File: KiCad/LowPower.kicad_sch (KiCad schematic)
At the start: 35 parts, among them J1 Connector, J2 USB-C, J3 DC, U1 ESP32-WROOM-32, U2 FT231XQ, U4 LMR16006+FB

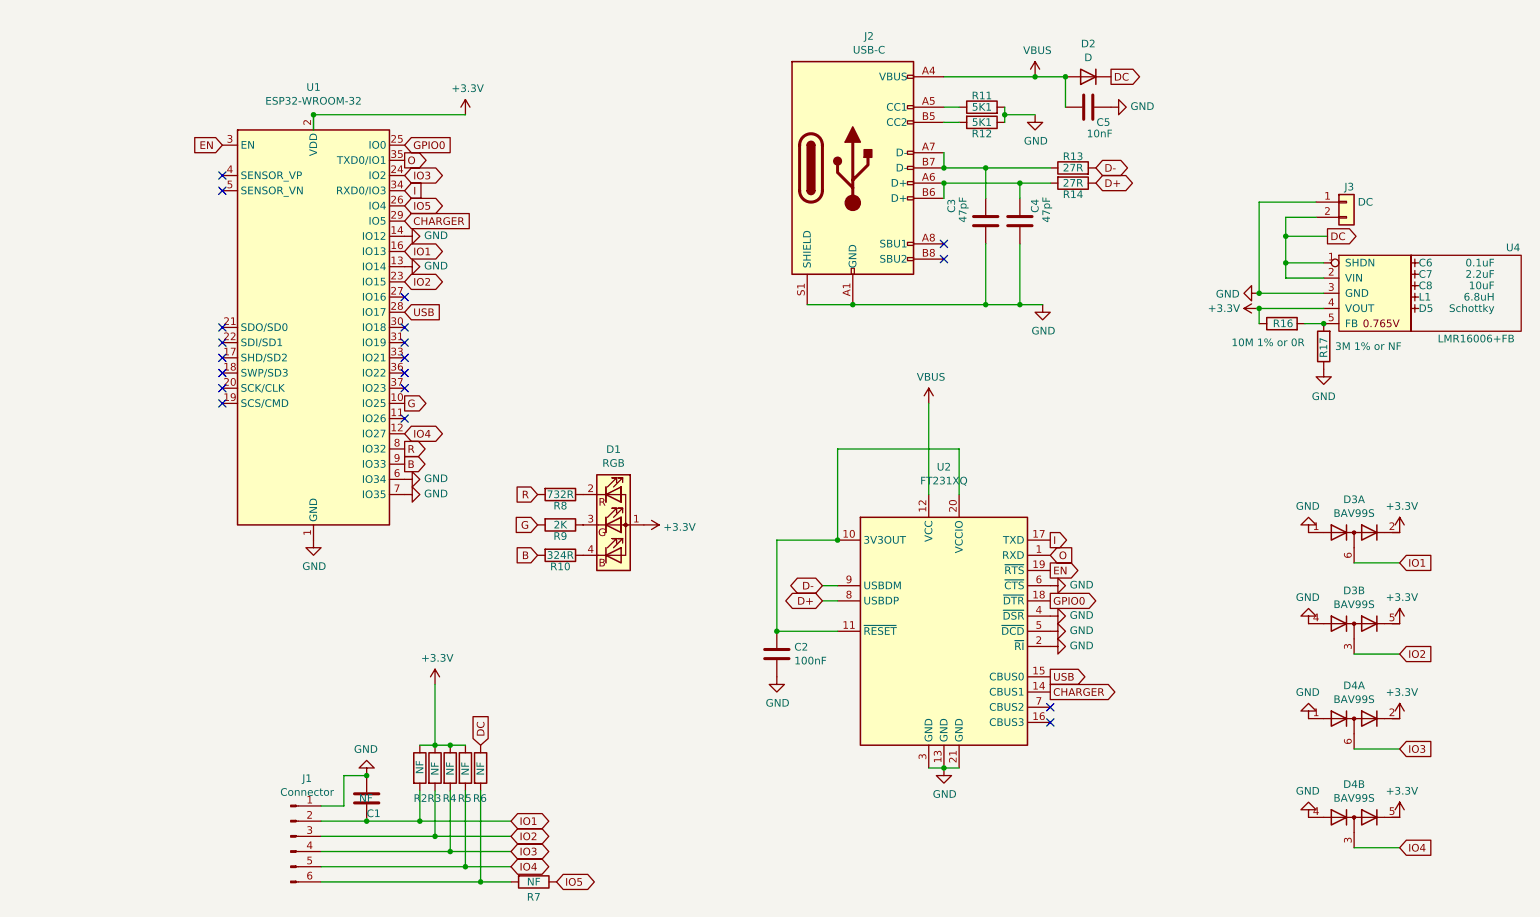
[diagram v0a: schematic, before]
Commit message: Separate Generic and LowPower boards
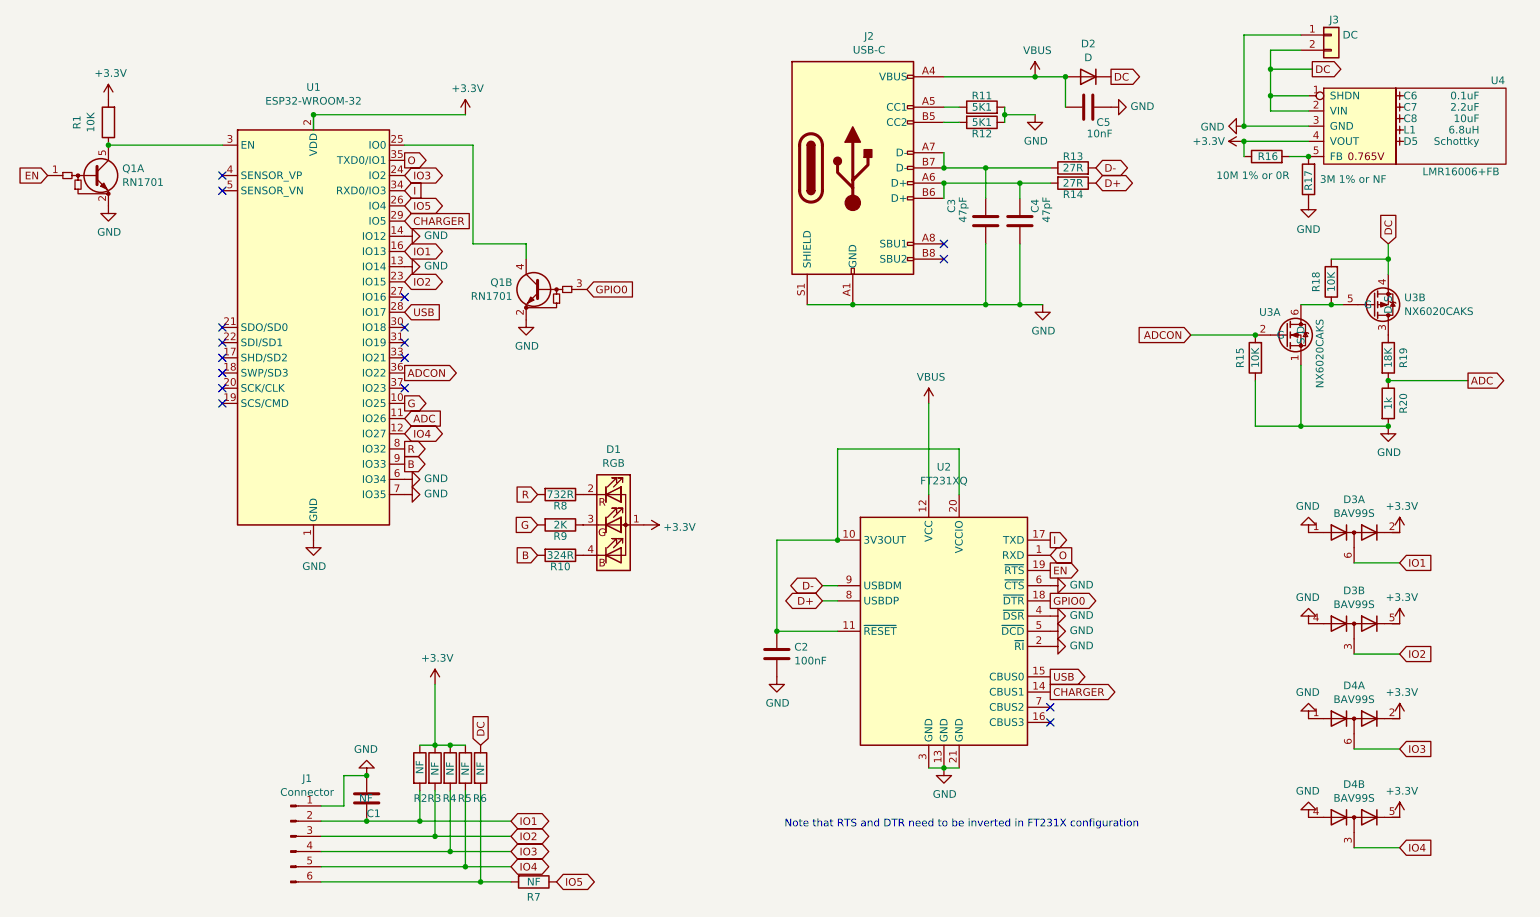
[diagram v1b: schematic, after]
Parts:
- added Q1: RN1701, RevK:USV-5, symbol RevK:RN1701
- added R1, R15, R18: 10K, RevK:R_0603, symbol Device:R
- added R19: 18K, RevK:R_0603, symbol Device:R
- added R20: 1k, RevK:R_0603, symbol Device:R
- added U3: NX6020CAKS, Package_TO_SOT_SMD:SOT-363_SC-70-6, symbol RevK:NX6020CAKS
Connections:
- net +3V3: now also R1.2
- net DC: now also R18.2, U3.4 (S)
- net EN: now also Q1.1 (B2); no longer U1.3 (EN)
- net GND: now also Q1.2 (E), Q1.2 (E), R15.1, R20.2, U3.1 (S)
- net GPIO0: now also Q1.3 (B2); no longer U1.25 (IO0)
- net ADC: now reaches U1.11 (IO26)
- net ADC: now also R19.2, R20.1
- net ADCON: now reaches U1.36 (IO22)
- net ADCON: now also R15.2, U3.2 (G)
- new net: Q1.4 (C2), U1.25 (IO0)
- new net: Q1.5 (C2), R1.1, U1.3 (EN)
- new net: R19.1, U3.3 (D)
- new net: R18.1, U3.5 (G), U3.6 (D)
- no-connect marks 19 -> 17
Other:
- note added: "Note that RTS and DTR need to be inverted in FT231X configuration"
- title: Generic ESP32 module -> Generic ESP32 (suitable for battery operation)
- moved on the sheet: C6, C7, C8, D5, J3, L1, R16, R17, U4

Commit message: New bigger generic and tidy library
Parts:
- C1, R2, R4, R5, R6, R7: footprint RevK:Pad_1206_0805_NF -> RevK:Pad_1206_0805_Open; now left out of the parts list
- R3: footprint RevK:Pad_1206_0805_NF -> RevK:Pad_1206_0805_Open
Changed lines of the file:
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@@
   )
   (symbol (lib_id "Device:R") (at 83.185 140.97 0) (unit 1)
-    (in_bom yes) (on_board yes)
+    (in_bom no) (on_board yes)
     (property "Reference" "R2" (id 0) (at 84.455 146.05 0)
       (effects (font (size 1.27 1.27)) (justify right))
@@
       (effects (font (size 1.27 1.27)) (justify right))
     )
-    (property "Footprint" "RevK:Pad_1206_0805_NF" (id 2) (at 81.407 140.97 90)
+    (property "Footprint" "RevK:Pad_1206_0805_Open" (id 2) (at 81.407 140.97 90)
       (effects (font (size 1.27 1.27)) hide)
     )
@@
       (effects (font (size 1.27 1.27)) (justify left))
     )
-    (property "Footprint" "RevK:Pad_1206_0805_NF" (id 2) (at 83.947 140.97 90)
+    (property "Footprint" "RevK:Pad_1206_0805_Open" (id 2) (at 83.947 140.97 90)
       (effects (font (size 1.27 1.27)) hide)
     )
@@
   )
   (symbol (lib_id "Device:R") (at 88.265 140.97 0) (unit 1)
-    (in_bom yes) (on_board yes)
+    (in_bom no) (on_board yes)
     (property "Reference" "R4" (id 0) (at 86.995 146.05 0)
       (effects (font (size 1.27 1.27)) (justify left))
@@
       (effects (font (size 1.27 1.27)) (justify left))
     )
-    (property "Footprint" "RevK:Pad_1206_0805_NF" (id 2) (at 86.487 140.97 90)
+    (property "Footprint" "RevK:Pad_1206_0805_Open" (id 2) (at 86.487 140.97 90)
       (effects (font (size 1.27 1.27)) hide)
     )
@@
   )
   (symbol (lib_id "Device:R") (at 90.805 140.97 0) (unit 1)
-    (in_bom yes) (on_board yes)
+    (in_bom no) (on_board yes)
     (property "Reference" "R5" (id 0) (at 89.535 146.05 0)
       (effects (font (size 1.27 1.27)) (justify left))
@@
       (effects (font (size 1.27 1.27)) (justify left))
     )
-    (property "Footprint" "RevK:Pad_1206_0805_NF" (id 2) (at 89.027 140.97 90)
+    (property "Footprint" "RevK:Pad_1206_0805_Open" (id 2) (at 89.027 140.97 90)
       (effects (font (size 1.27 1.27)) hide)
     )
@@
   )
   (symbol (lib_id "Device:R") (at 93.345 140.97 0) (unit 1)
-    (in_bom yes) (on_board yes)
+    (in_bom no) (on_board yes)
     (property "Reference" "R6" (id 0) (at 92.075 146.05 0)
       (effects (font (size 1.27 1.27)) (justify left))
@@
       (effects (font (size 1.27 1.27)) (justify left))
     )
-    (property "Footprint" "RevK:Pad_1206_0805_NF" (id 2) (at 91.567 140.97 90)
+    (property "Footprint" "RevK:Pad_1206_0805_Open" (id 2) (at 91.567 140.97 90)
       (effects (font (size 1.27 1.27)) hide)
     )
@@
   )
   (symbol (lib_id "Device:R") (at 102.235 160.02 270) (unit 1)
-    (in_bom yes) (on_board yes)
+    (in_bom no) (on_board yes)
     (property "Reference" "R7" (id 0) (at 102.235 162.56 90))
     (property "Value" "NF" (id 1) (at 102.235 160.02 90))
-    (property "Footprint" "RevK:Pad_1206_0805_NF" (id 2) (at 102.235 158.242 90)
+    (property "Footprint" "RevK:Pad_1206_0805_Open" (id 2) (at 102.235 158.242 90)
       (effects (font (size 1.27 1.27)) hide)
     )
@@
   )
   (symbol (lib_id "Device:C") (at 74.295 146.05 0) (unit 1)
-    (in_bom yes) (on_board yes)
+    (in_bom no) (on_board yes)
     (property "Reference" "C1" (id 0) (at 74.295 148.59 0)
       (effects (font (size 1.27 1.27)) (justify left))
@@
       (effects (font (size 1.27 1.27)) (justify left))
     )
-    (property "Footprint" "RevK:Pad_1206_0805_NF" (id 2) (at 75.2602 149.86 0)
+    (property "Footprint" "RevK:Pad_1206_0805_Open" (id 2) (at 75.2602 149.86 0)
       (effects (font (size 1.27 1.27)) hide)
     )
@@
     )
     (path "/00000000-0000-0000-0000-000060d24a40"
-      (reference "C1") (unit 1) (value "NF") (footprint "RevK:Pad_1206_0805_NF")
+      (reference "C1") (unit 1) (value "NF") (footprint "RevK:Pad_1206_0805_Open")
     )
     (path "/00000000-0000-0000-0000-0000609259a6"
@@
     )
     (path "/00000000-0000-0000-0000-00006043ffad"
-      (reference "R2") (unit 1) (value "NF") (footprint "RevK:Pad_1206_0805_NF")
+      (reference "R2") (unit 1) (value "NF") (footprint "RevK:Pad_1206_0805_Open")
     )
     (path "/00000000-0000-0000-0000-00006043ffb3"
-      (reference "R3") (unit 1) (value "NF") (footprint "RevK:Pad_1206_0805_NF")
+      (reference "R3") (unit 1) (value "NF") (footprint "RevK:Pad_1206_0805_Open")
     )
     (path "/00000000-0000-0000-0000-00006043ffb9"
-      (reference "R4") (unit 1) (value "NF") (footprint "RevK:Pad_1206_0805_NF")
+      (reference "R4") (unit 1) (value "NF") (footprint "RevK:Pad_1206_0805_Open")
     )
     (path "/00000000-0000-0000-0000-000060d24a3a"
-      (reference "R5") (unit 1) (value "NF") (footprint "RevK:Pad_1206_0805_NF")
+      (reference "R5") (unit 1) (value "NF") (footprint "RevK:Pad_1206_0805_Open")
     )
     (path "/00000000-0000-0000-0000-000060d24a3b"
-      (reference "R6") (unit 1) (value "NF") (footprint "RevK:Pad_1206_0805_NF")
+      (reference "R6") (unit 1) (value "NF") (footprint "RevK:Pad_1206_0805_Open")
     )
     (path "/00000000-0000-0000-0000-000060d24a3f"
-      (reference "R7") (unit 1) (value "NF") (footprint "RevK:Pad_1206_0805_NF")
+      (reference "R7") (unit 1) (value "NF") (footprint "RevK:Pad_1206_0805_Open")
     )
     (path "/00000000-0000-0000-0000-000060cf9e4d"

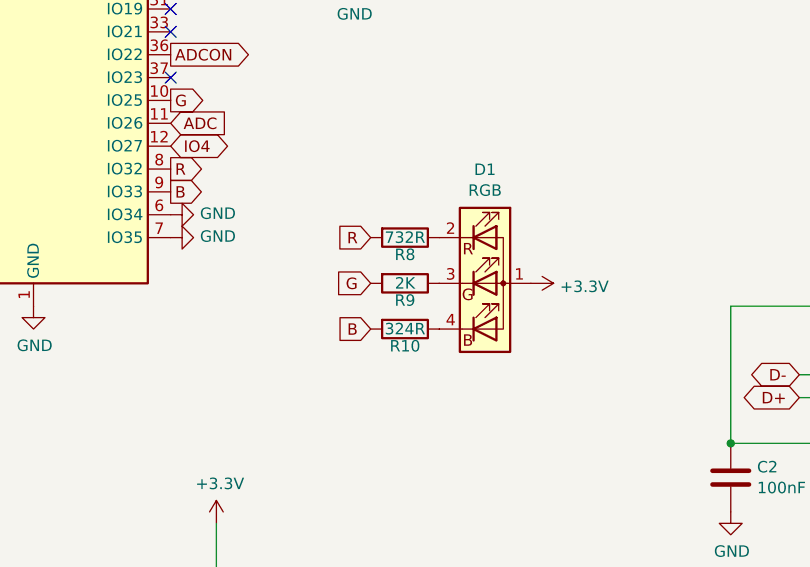
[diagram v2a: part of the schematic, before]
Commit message: Lots of tidy - mainly silkscreen stuff
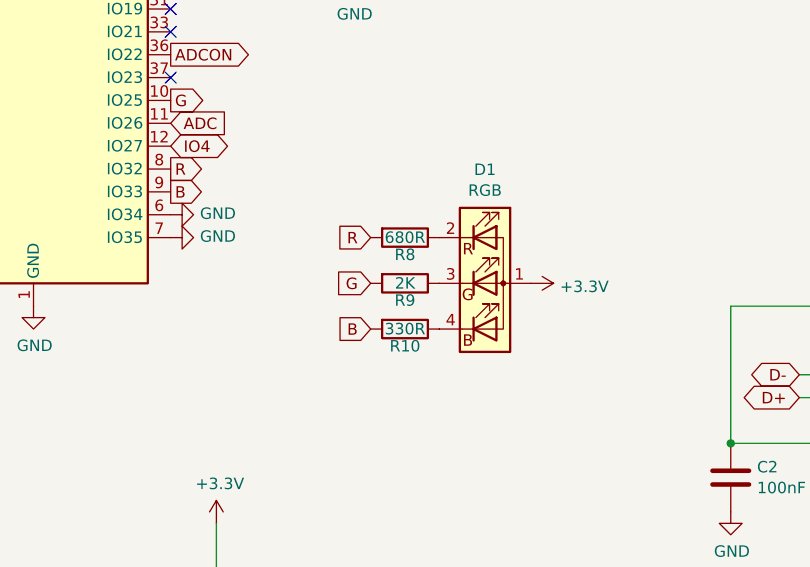
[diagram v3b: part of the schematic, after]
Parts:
- J1: footprint RevK:Molex_MiniSPOX_H6RA_0.1 -> RevK:Molex_MiniSPOX_H6RA
- R10: value 324R -> 330R
- R8: value 732R -> 680R
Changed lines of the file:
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@@
     (in_bom yes) (on_board yes)
     (property "Reference" "R10" (id 0) (at 106.68 107.315 90))
-    (property "Value" "324R" (id 1) (at 106.68 105.41 90))
+    (property "Value" "330R" (id 1) (at 106.68 105.41 90))
     (property "Footprint" "RevK:R_0603" (id 2) (at 106.68 103.632 90)
       (effects (font (size 1.27 1.27)) hide)
@@
     (in_bom yes) (on_board yes)
     (property "Reference" "R8" (id 0) (at 106.68 97.155 90))
-    (property "Value" "732R" (id 1) (at 106.68 95.25 90))
+    (property "Value" "680R" (id 1) (at 106.68 95.25 90))
     (property "Footprint" "RevK:R_0603" (id 2) (at 106.68 93.472 90)
       (effects (font (size 1.27 1.27)) hide)
@@
     (property "Reference" "J1" (id 0) (at 64.3382 142.7226 0))
     (property "Value" "Connector" (id 1) (at 64.3382 145.034 0))
-    (property "Footprint" "RevK:Molex_MiniSPOX_H6RA_0.1" (id 2) (at 61.595 152.4 0)
+    (property "Footprint" "RevK:Molex_MiniSPOX_H6RA" (id 2) (at 61.595 152.4 0)
       (effects (font (size 1.27 1.27)) hide)
     )
@@
     )
     (path "/00000000-0000-0000-0000-000060d24a3c"
-      (reference "J1") (unit 1) (value "Connector") (footprint "RevK:Molex_MiniSPOX_H6RA_0.1")
+      (reference "J1") (unit 1) (value "Connector") (footprint "RevK:Molex_MiniSPOX_H6RA")
     )
     (path "/00000000-0000-0000-0000-000060d24a36"
@@
     )
     (path "/00000000-0000-0000-0000-000060cf9e4d"
-      (reference "R8") (unit 1) (value "732R") (footprint "RevK:R_0603")
+      (reference "R8") (unit 1) (value "680R") (footprint "RevK:R_0603")
     )
     (path "/00000000-0000-0000-0000-000060cfbfaf"
@@
     )
     (path "/00000000-0000-0000-0000-000060a436c8"
-      (reference "R10") (unit 1) (value "324R") (footprint "RevK:R_0603")
+      (reference "R10") (unit 1) (value "330R") (footprint "RevK:R_0603")
     )
     (path "/00000000-0000-0000-0000-00006043a8ad"

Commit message: Footprint update
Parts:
- removed U2: FT231XQ, RevK:QFN-20-1EP_4x4mm_P0.5mm_EP2.5x2.5mm, symbol Interface_USB:FT231XQ
- added U2: FT231XQ, RevK:QFN-20-1EP_4x4mm_P0.5mm_EP2.5x2.5mm, symbol RevK:FT231XQ
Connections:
- net CHARGER: now also U2.14 (CBUS1)
- net D+: now also U2.8 (USBDP)
- net D-: now also U2.9 (USBDM)
- net EN: now also U2.19 (~{RTS})
- net GND: now also U2.13 (GND), U2.2 (~{RI}), U2.21 (GND), U2.3 (GND), U2.4 (~{DSR}), U2.5 (~{DCD}), U2.6 (~{CTS})
- net GPIO0: now also U2.18 (~{DTR})
- net I: now also U2.17 (TXD)
- net O: now also U2.1 (RXD)
- net USB: now also U2.15 (CBUS0)
- net VBUS: now also U2.12 (VCC)
- net at C2.1: now also U2.10 (3V3OUT), U2.11 (~{RESET}), U2.20 (VCCIO)
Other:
- moved on the sheet: C2

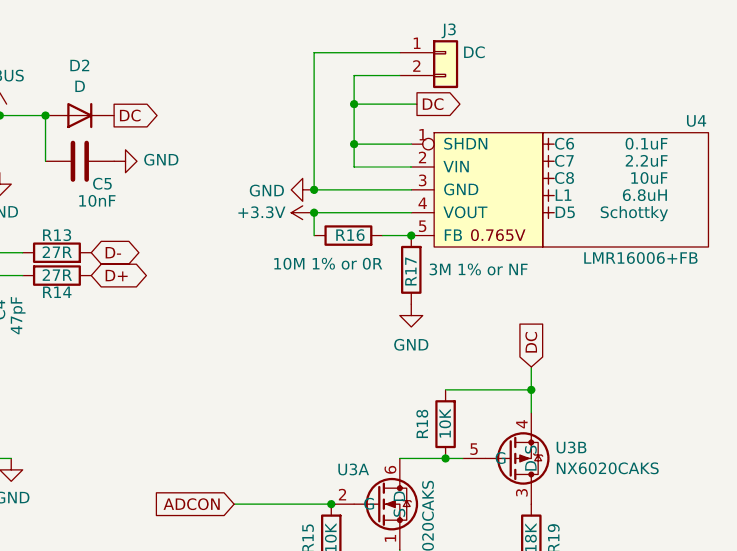
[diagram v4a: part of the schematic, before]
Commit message: Change resistor values
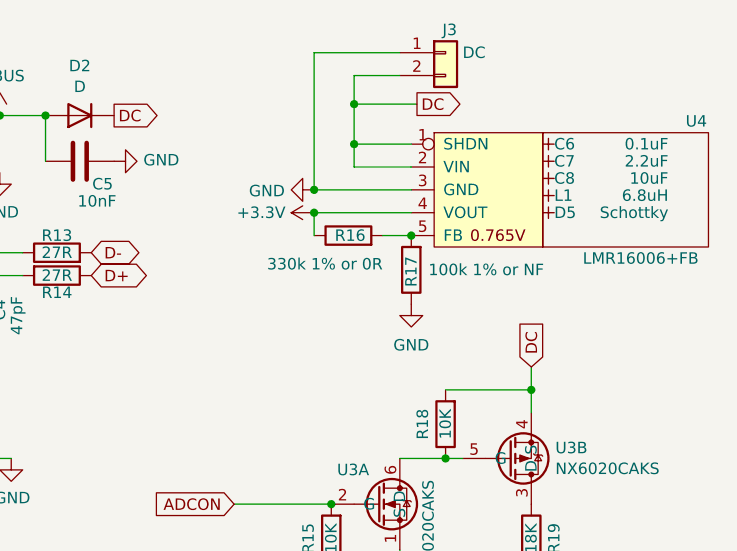
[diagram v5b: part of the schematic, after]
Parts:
- R16: value 10M 1% or 0R -> 330k 1% or 0R
- R17: value 3M 1% or NF -> 100k 1% or NF
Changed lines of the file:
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@@
       (effects (font (size 1.27 1.27)) (justify right))
     )
-    (property "Value" "3M 1% or NF" (id 1) (at 233.68 42.545 0)
+    (property "Value" "100k 1% or NF" (id 1) (at 233.68 42.545 0)
       (effects (font (size 1.27 1.27)) (justify right))
     )
@@
       (effects (font (size 1.27 1.27)) (justify left))
     )
-    (property "Value" "10M 1% or 0R" (id 1) (at 228.6 41.91 90)
+    (property "Value" "330k 1% or 0R" (id 1) (at 228.6 41.91 90)
       (effects (font (size 1.27 1.27)) (justify left))
     )
@@
     )
     (path "/fc3ca677-79f2-42b6-a5b3-ff3b18df1d6c"
-      (reference "R16") (unit 1) (value "10M 1% or 0R") (footprint "RevK:R_0603")
+      (reference "R16") (unit 1) (value "330k 1% or 0R") (footprint "RevK:R_0603")
     )
     (path "/83151023-5106-4495-aeff-aefc75dfd6c0"
-      (reference "R17") (unit 1) (value "3M 1% or NF") (footprint "RevK:R_0603")
+      (reference "R17") (unit 1) (value "100k 1% or NF") (footprint "RevK:R_0603")
     )
     (path "/00000000-0000-0000-0000-000060ab0248"
